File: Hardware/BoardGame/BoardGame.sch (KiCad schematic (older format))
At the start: 3 parts

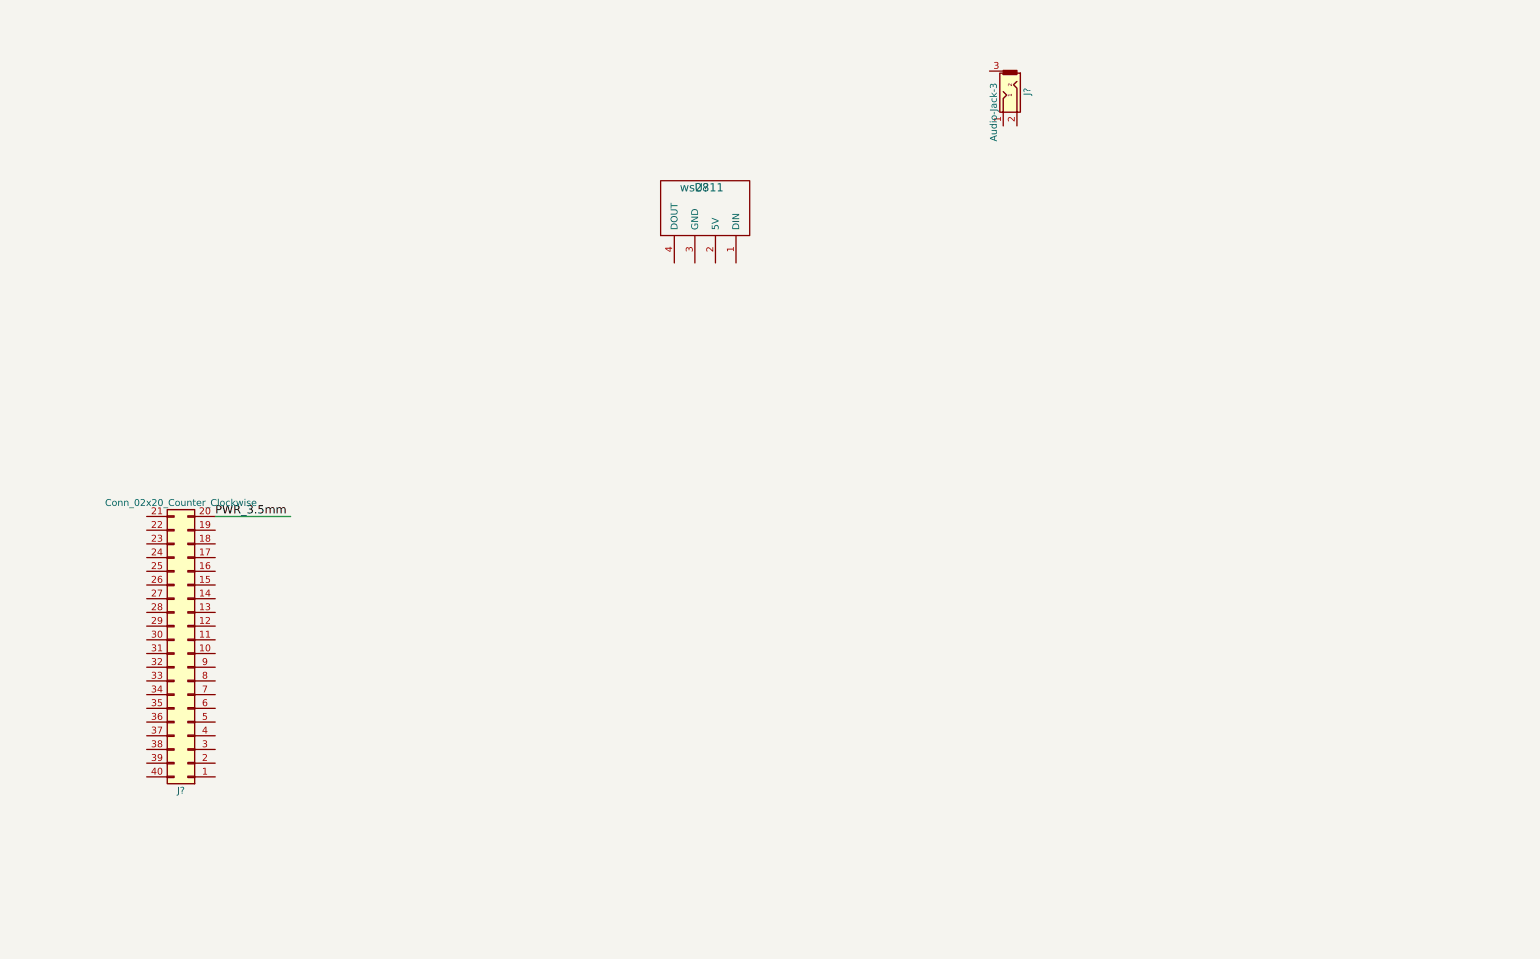
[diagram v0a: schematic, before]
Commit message: add RPi connections, pawn assembly
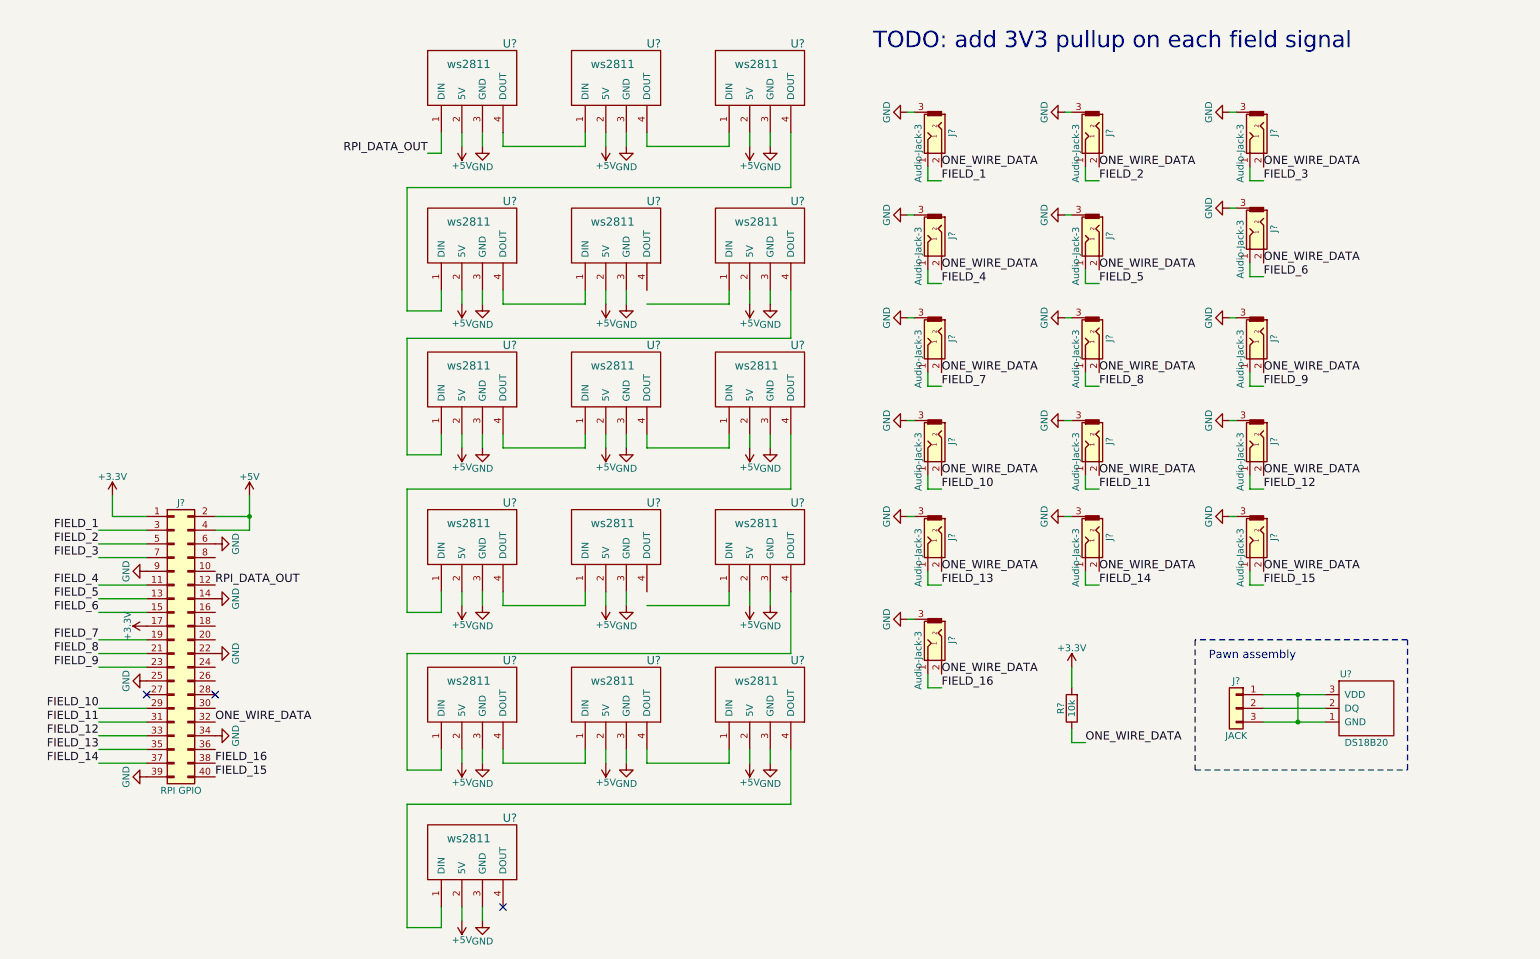
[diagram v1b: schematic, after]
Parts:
- removed J?: Conn_02x20_Counter_Clockwise, symbol Conn_02x20_Counter_Clockwise
- removed U?: ws2811, symbol ws2811
- added J? (x15): Audio-Jack-3, symbol Audio-Jack-3
- added J?: JACK, symbol Conn_01x03
- added J?: RPI GPIO, symbol Conn_02x20_Odd_Even
- added R?: 10k, symbol R
- added U? (x16): ws2811, symbol ws2811
- added U?: DS18B20, symbol DS18B20
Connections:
- net labels added: +3.3V, +5V, FIELD_1, FIELD_10, FIELD_11, FIELD_12, FIELD_13, FIELD_14, FIELD_15, FIELD_16, FIELD_2, FIELD_3, FIELD_4, FIELD_5, FIELD_6, FIELD_7, FIELD_8, FIELD_9, GND, ONE_WIRE_DATA, RPI_DATA_OUT
- net labels removed: PWR_3.5mm
- wire segments 1 -> 161
- no-connect marks 0 -> 3
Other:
- note added: "Pawn assembly"
- note added: "TODO: add 3V3 pullup on each field signal"
- moved on the sheet: J?

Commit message: annotate schematic, add pdf export
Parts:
- R1: renamed from R?; value 10k -> 4k7
- gave numbers to parts that had none: 35
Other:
- note added: "Pin numbers on J17\nmatch those on J1..J16"
- moved on the sheet: J17, R1, U17

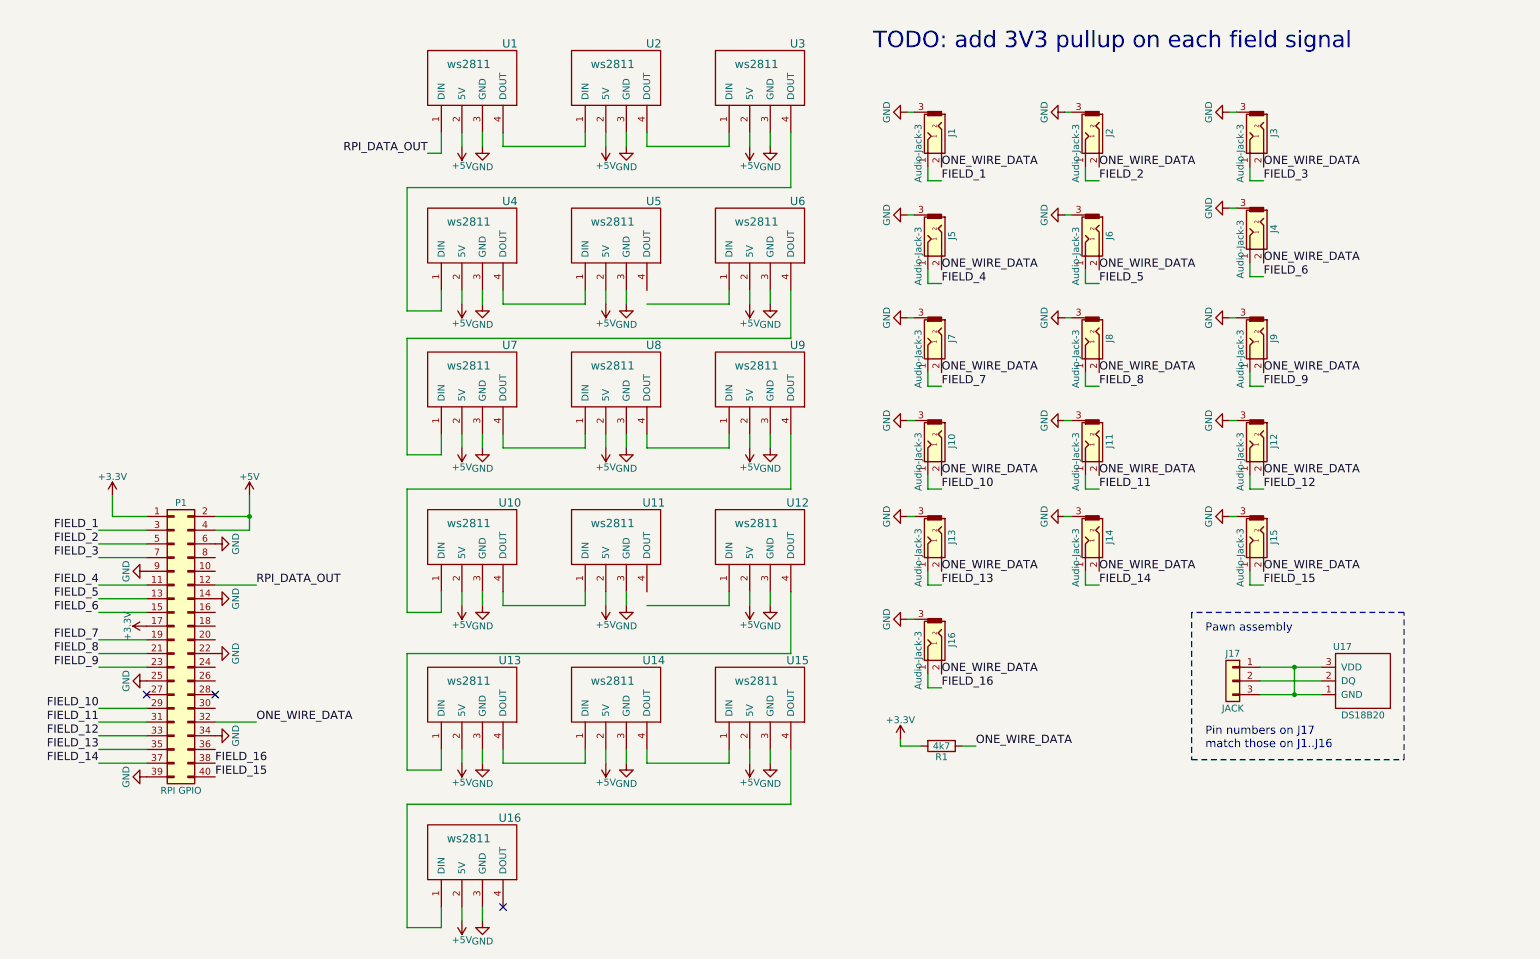
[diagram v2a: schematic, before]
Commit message: add missing pullups and buttons, remove unknowns
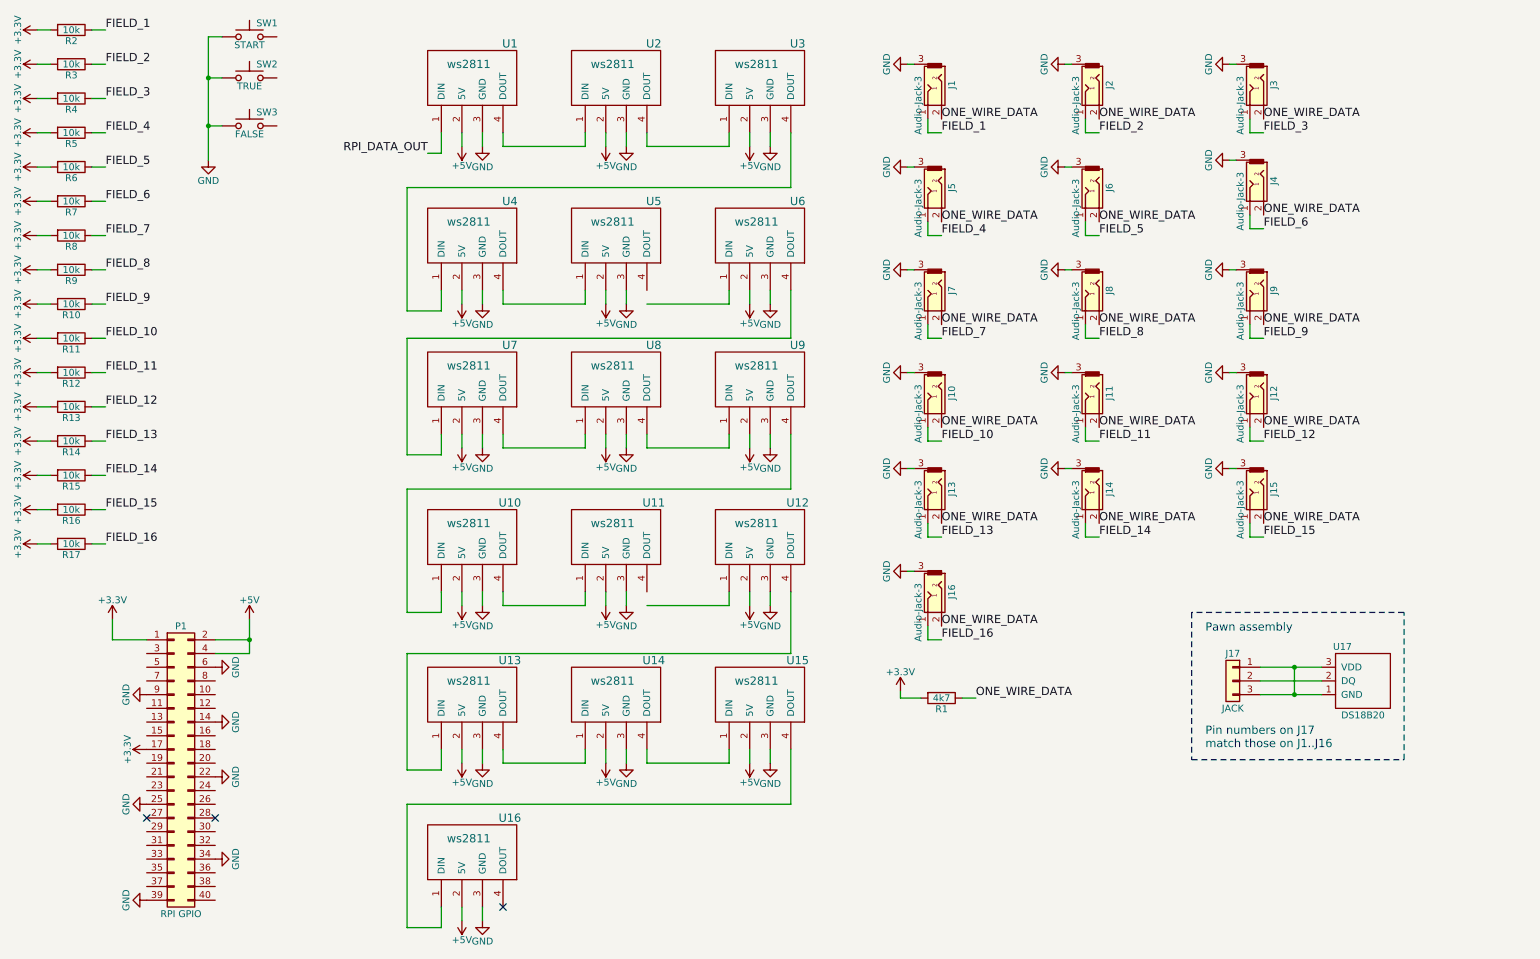
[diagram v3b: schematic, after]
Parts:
- added R10, R11, R12, R13, R14, R15, R16, R17, R2, R3, R4, R5, R6, R7, R8, R9: 10k, symbol R
- added SW1: START, symbol SW_Push
- added SW2: TRUE, symbol SW_Push
- added SW3: FALSE, symbol SW_Push
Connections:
- net +3V3: now also R10.2, R11.2, R12.2, R13.2, R14.2, R15.2, R16.2, R17.2, R2.2, R3.2, R4.2, R5.2, R6.2, R7.2, R8.2, R9.2
- net FIELD_1: now also R2.1; no longer P1.3 (Pin_3)
- net FIELD_10: now also R11.1; no longer P1.29 (Pin_29)
- net FIELD_11: now also R12.1; no longer P1.31 (Pin_31)
- net FIELD_12: now also R13.1; no longer P1.33 (Pin_33)
- net FIELD_13: now also R14.1; no longer P1.35 (Pin_35)
- net FIELD_14: now also R15.1; no longer P1.37 (Pin_37)
- net FIELD_15: now also R16.1; no longer P1.40 (Pin_40)
- net FIELD_16: now also R17.1; no longer P1.38 (Pin_38)
- net FIELD_2: now also R3.1; no longer P1.5 (Pin_5)
- net FIELD_3: now also R4.1; no longer P1.7 (Pin_7)
- net FIELD_4: now also R5.1; no longer P1.11 (Pin_11)
- net FIELD_5: now also R6.1; no longer P1.13 (Pin_13)
- net FIELD_6: now also R7.1; no longer P1.15 (Pin_15)
- net FIELD_7: now also R8.1; no longer P1.19 (Pin_19)
- net FIELD_8: now also R9.1; no longer P1.21 (Pin_21)
- net FIELD_9: now also R10.1; no longer P1.23 (Pin_23)
- net GND: now also SW1.1, SW2.1, SW3.1
- net ONE_WIRE_DATA: no longer P1.32 (Pin_32)
- net RPI_DATA_OUT: no longer P1.12 (Pin_12)
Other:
- note removed: "TODO: add 3V3 pullup on each field signal"
- moved on the sheet: J1, J10, J11, J12, J13, J14, J15, J16, J2, J3, J4, J5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
